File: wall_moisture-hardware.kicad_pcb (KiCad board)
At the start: 4 copper layers, 78.5 x 99.3 mm, 46 parts, among them SW2 FSMH

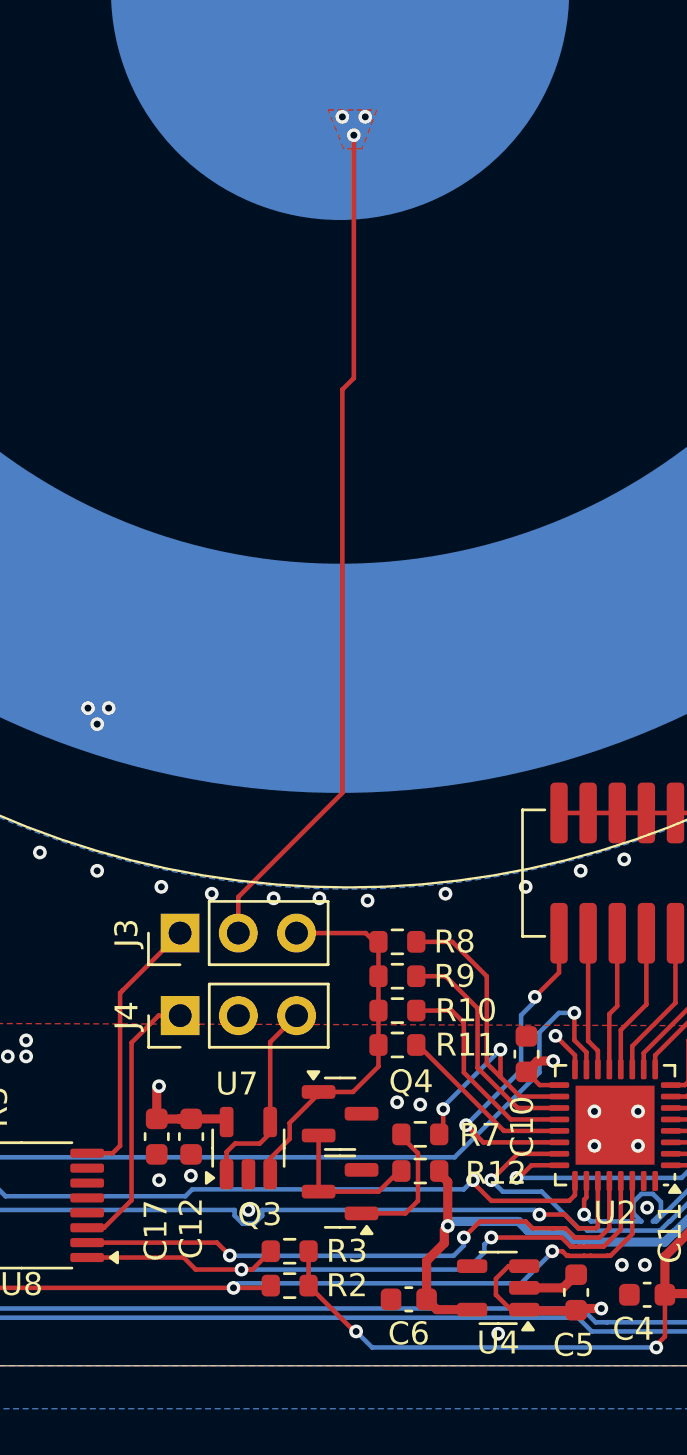
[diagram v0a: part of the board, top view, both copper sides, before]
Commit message: design: Shield excitation signal and exclude poor planes around the signal trace
Excluding poor plane around the signal should reduce the capacitive parasitance.
Shield is now protecting the signal trace that goes to the electrode
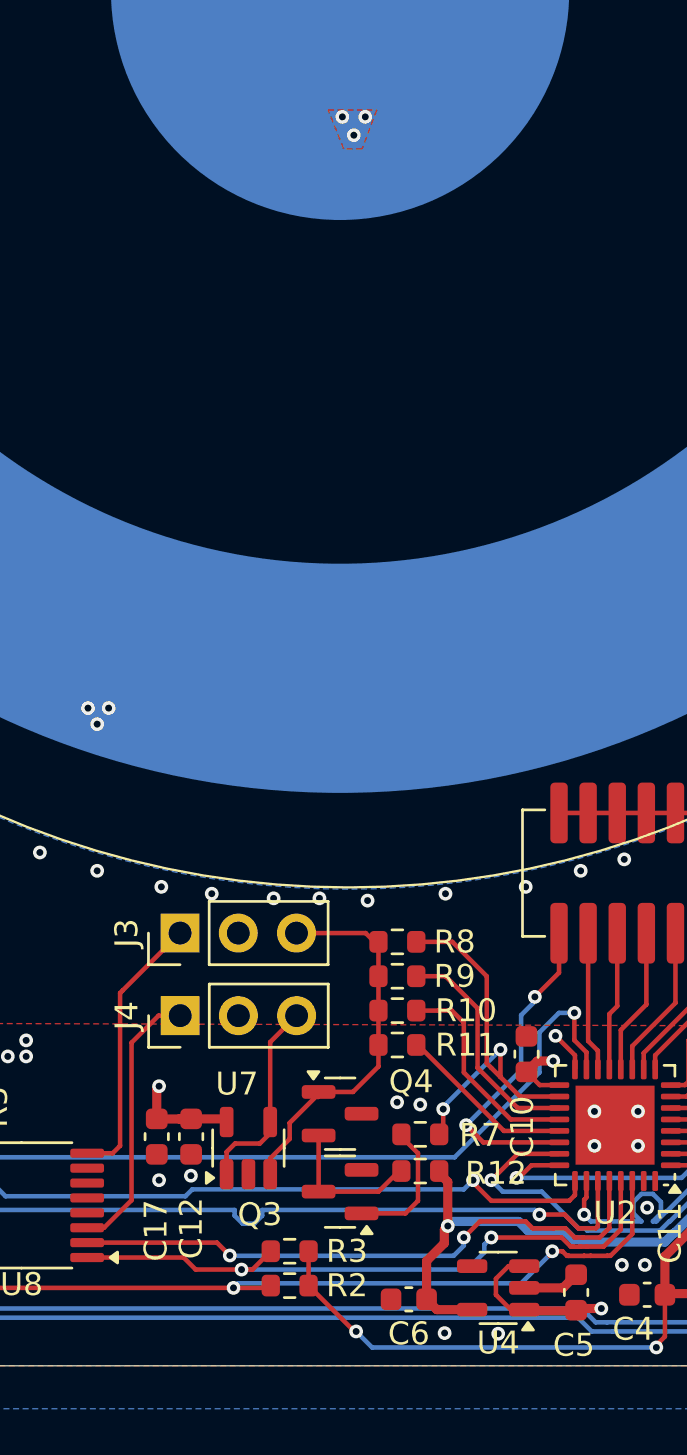
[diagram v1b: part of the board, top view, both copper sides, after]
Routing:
- added copper zone on In1.Cu, net /Analog frontend/SENSOR_SHIELD
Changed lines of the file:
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@@
 	)
 	(via
-		(at 92.338439 132.727778)
+		(at 85.338439 110.827778)
 		(size 0.6)
 		(drill 0.3)
@@
 	)
 	(via
-		(at 85.338439 110.827778)
+		(at 125.538439 125.227778)
 		(size 0.6)
 		(drill 0.3)
@@
 	)
 	(via
-		(at 125.538439 125.227778)
+		(at 66.038439 133.127778)
 		(size 0.6)
 		(drill 0.3)
@@
 	)
 	(via
-		(at 66.038439 133.127778)
+		(at 127.338439 132.527778)
 		(size 0.6)
 		(drill 0.3)
@@
 	)
 	(via
-		(at 127.338439 132.527778)
+		(at 100.9 138.1)
 		(size 0.6)
 		(drill 0.3)
@@
 	)
 	(segment
+		(start 91.896229 120.644614)
+		(end 91.938439 120.602404)
+		(width 0.8)
+		(layer "F.Cu")
+		(net 18)
+	)
+	(via
+		(at 96.938439 85.827778)
+		(size 0.6)
+		(drill 0.3)
+		(layers "F.Cu" "B.Cu")
+		(net 18)
+	)
+	(via
+		(at 97.438439 85.027778)
+		(size 0.6)
+		(drill 0.3)
+		(layers "F.Cu" "B.Cu")
+		(net 18)
+	)
+	(via
+		(at 96.438439 85.027778)
+		(size 0.6)
+		(drill 0.3)
+		(layers "F.Cu" "B.Cu")
+		(net 18)
+	)
+	(segment
 		(start 91.896229 119.069988)
 		(end 96.438439 114.527778)
 		(width 0.2)
-		(layer "F.Cu")
+		(layer "In2.Cu")
 		(net 18)
 	)
@@
 		(end 96.438439 96.927778)
 		(width 0.2)
-		(layer "F.Cu")
+		(layer "In2.Cu")
 		(net 18)
 	)
@@
 		(end 91.896229 119.069988)
 		(width 0.2)
-		(layer "F.Cu")
-		(net 18)
-	)
-	(segment
-		(start 91.896229 120.644614)
-		(end 91.938439 120.602404)
-		(width 0.8)
-		(layer "F.Cu")
+		(layer "In2.Cu")
 		(net 18)
 	)
@@
 		(end 96.938439 86.027778)
 		(width 0.2)
-		(layer "F.Cu")
+		(layer "In2.Cu")
 		(net 18)
 	)
@@
 		(end 96.938439 96.427778)
 		(width 0.2)
-		(layer "F.Cu")
-		(net 18)
-	)
-	(via
-		(at 96.938439 85.827778)
-		(size 0.6)
-		(drill 0.3)
-		(layers "F.Cu" "B.Cu")
-		(net 18)
-	)
-	(via
-		(at 97.438439 85.027778)
-		(size 0.6)
-		(drill 0.3)
-		(layers "F.Cu" "B.Cu")
-		(net 18)
-	)
-	(via
-		(at 96.438439 85.027778)
-		(size 0.6)
-		(drill 0.3)
-		(layers "F.Cu" "B.Cu")
+		(layer "In2.Cu")
 		(net 18)
 	)
@@
 	)
 	(zone
+		(net 0)
+		(net_name "")
+		(layers "F.Cu" "In1.Cu" "In2.Cu")
+		(hatch edge 0.5)
+		(connect_pads
+			(clearance 0)
+		)
+		(min_thickness 0.25)
+		(filled_areas_thickness no)
+		(keepout
+			(tracks allowed)
+			(vias allowed)
+			(pads allowed)
+			(copperpour not_allowed)
+			(footprints allowed)
+		)
+		(placement
+			(enabled no)
+			(sheetname "/Analog frontend/")
+		)
+		(fill
+			(thermal_gap 0.5)
+			(thermal_bridge_width 0.5)
+		)
+		(polygon
+			(pts
+				(xy 83.6 129.5) (xy 83.6 130.8) (xy 87.2 130.8) (xy 87.3 130.7) (xy 87.3 123.8) (xy 89.7 121.4)
+				(xy 90.9 121.4) (xy 90.7 121.2) (xy 87.7 121.2) (xy 85.9 123) (xy 85.9 129.4) (xy 85.8 129.5)
+			)
+		)
+	)
+	(zone
+		(net 0)
+		(net_name "")
+		(layers "F.Cu" "In1.Cu" "In2.Cu")
+		(hatch edge 0.5)
+		(connect_pads
+			(clearance 0)
+		)
+		(min_thickness 0.25)
+		(filled_areas_thickness no)
+		(keepout
+			(tracks allowed)
+			(vias allowed)
+			(pads allowed)
+			(copperpour not_allowed)
+			(footprints allowed)
+		)
+		(placement
+			(enabled no)
+			(sheetname "/Analog frontend/")
+		)
+		(fill
+			(thermal_gap 0.5)
+			(thermal_bridge_width 0.5)
+		)
+		(polygon
+			(pts
+				(xy 93.1 122.4) (xy 93.2 122.5) (xy 97 122.5) (xy 97 126.3) (xy 96.9 126.4) (xy 97.2 126.7) (xy 100.2 126.7)
+				(xy 103 129.5) (xy 106.7 129.5) (xy 106.7 127.3) (xy 106.5 127.1) (xy 104 127.1) (xy 103.9 127)
+				(xy 103.9 124.9) (xy 103.2 124.9) (xy 103.2 121.8) (xy 100.8 119.4) (xy 87.9 119.4) (xy 87.8 119.5)
+				(xy 87.8 122.1) (xy 88.2 122.5) (xy 93.2 122.5)
+			)
+		)
+	)
+	(zone
+		(net 0)
+		(net_name "")
+		(layers "F.Cu" "In1.Cu" "In2.Cu")
+		(hatch edge 0.5)
+		(connect_pads
+			(clearance 0)
+		)
+		(min_thickness 0.25)
+		(filled_areas_thickness no)
+		(keepout
+			(tracks allowed)
+			(vias allowed)
+			(pads allowed)
+			(copperpour not_allowed)
+			(footprints allowed)
+		)
+		(placement
+			(enabled no)
+			(sheetname "/Analog frontend/")
+		)
+		(fill
+			(thermal_gap 0.5)
+			(thermal_bridge_width 0.5)
+		)
+		(polygon
+			(pts
+				(xy 92.8 132.1) (xy 93.7 132.1) (xy 94 131.8) (xy 94 130.3) (xy 94.7 129.6) (xy 94.7 129) (xy 95.8 129)
+				(xy 96.338439 128.461561) (xy 96.338439 128) (xy 97.9 128) (xy 98.9 127) (xy 98.9 126.3) (xy 98.8 126.2)
+				(xy 94.6 126.2) (xy 92.8 128) (xy 92.8 130.8)
+			)
+		)
+	)
+	(zone
 		(net 9)
 		(net_name "/Analog frontend/SENSOR_SHIELD")
@@
 			)
 		)
+	)
+	(zone
+		(net 9)
+		(net_name "/Analog frontend/SENSOR_SHIELD")
+		(layer "In1.Cu")
+		(hatch edge 0.5)
+		(priority 1)
+		(connect_pads
+			(clearance 0.2)
+		)
+		(min_thickness 0.25)
+		(filled_areas_thickness no)
+		(fill yes
+			(thermal_gap 0.5)
+			(thermal_bridge_width 0.5)
+		)
+		(polygon
+			(pts
+				(xy 99.2 83.5) (xy 99.3 114.9) (xy 93.6 121.8) (xy 93.6 125.6) (xy 90 125.6) (xy 90 121.797379)
+				(xy 90.6 118.4) (xy 94.2 113.9) (xy 94.6 83.6)
+			)
+		)

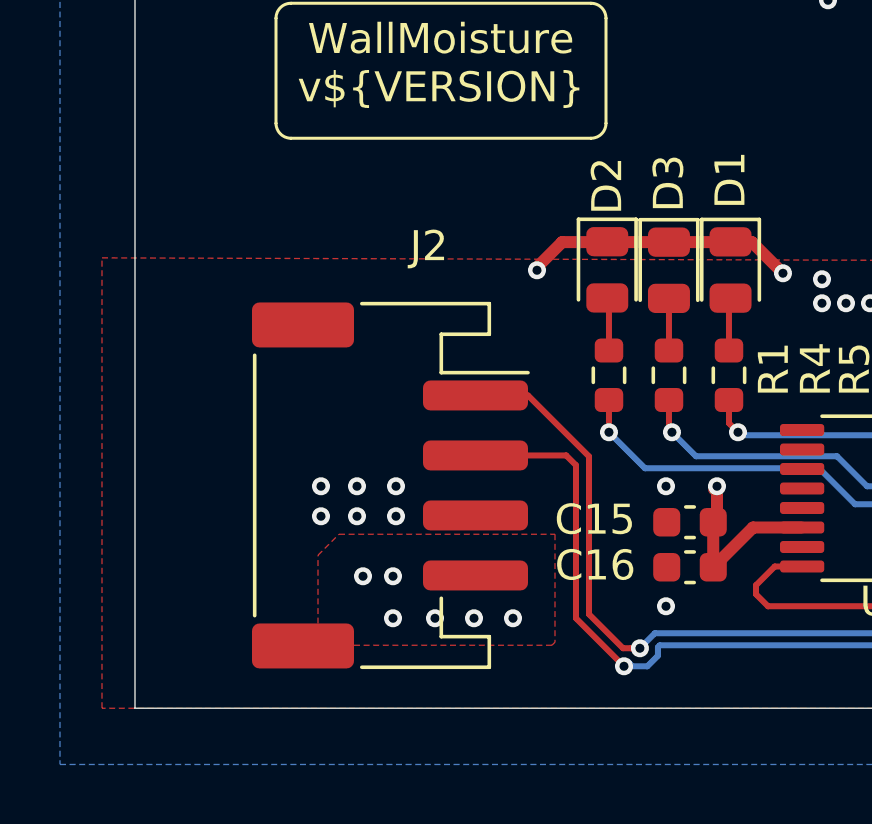
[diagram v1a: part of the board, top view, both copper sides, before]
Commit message: design: Align interface connectors
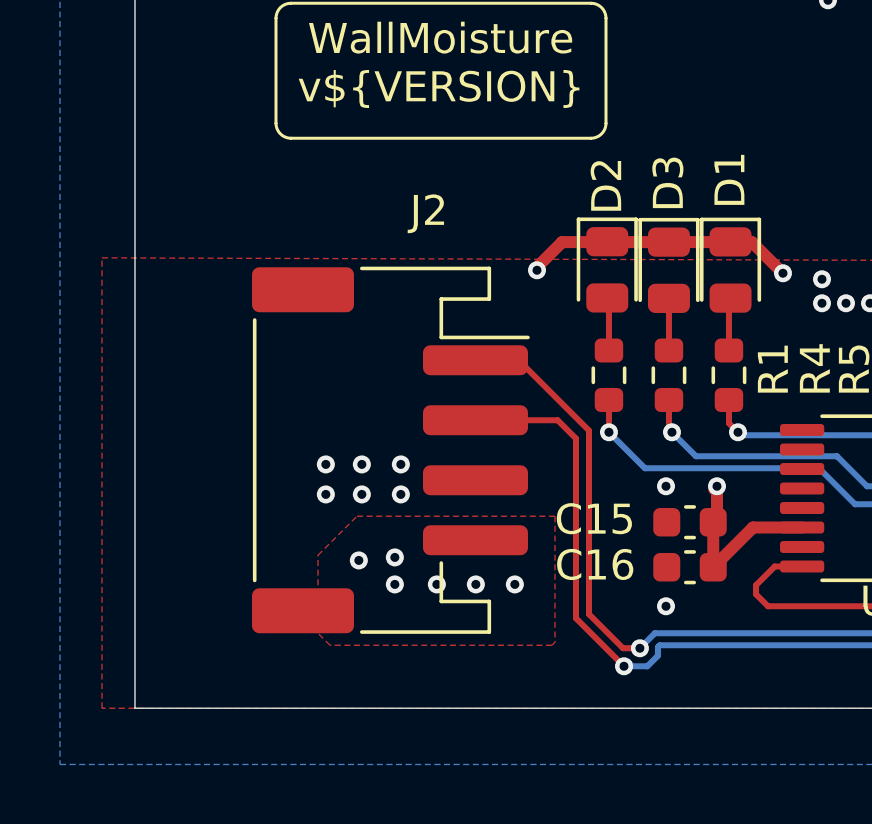
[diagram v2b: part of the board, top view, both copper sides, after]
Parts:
- moved J2 1.17 mm to (65.8, 130.9)
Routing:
- net /Connectors and Power/MASTER_TX: track 91.4 -> 92.4 mm
- net /Connectors and Power/MASTER_RX: track 84.2 -> 85.2 mm
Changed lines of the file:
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@@
 	(footprint "footprints:JST_PH_S4B-PH-SM4-TB_1x04-1MP_P2.00mm_Horizontal"
 		(layer "F.Cu")
-		(at 65.838439 132.101263 -90)
+		(at 65.838439 130.927778 -90)
 		(descr "JST PH series connector, S4B-PH-SM4-TB (http://www.jst-mfg.com/product/pdf/eng/ePH.pdf), generated with kicad-footprint-generator")
 		(tags "connector JST PH horizontal")
 		(property "Reference" "J2"
-			(at -7.973485 -1.3 180)
+			(at -7.973485 -1.3 0)
 			(layer "F.SilkS")
 			(effects
@@
 			(at 0 5.8 90)
 			(layer "F.Fab")
+			(hide yes)
 			(effects
 				(font
@@
 			(layer "F.Fab")
 		)
-		(fp_text user "${REFERENCE}"
-			(at 0 1.5 90)
-			(layer "F.Fab")
-			(effects
-				(font
-					(size 1 1)
-					(thickness 0.15)
-				)
-			)
-		)
 		(pad "1" smd roundrect
 			(at -3 -2.85 270)
@@
 		(sheetname "/Analog frontend/")
 		(sheetfile "analog_front_end.kicad_sch")
-		(attr smd exclude_from_bom dnp)
+		(attr smd exclude_from_bom)
 		(fp_text user "${REFERENCE}"
 			(at 0 -2.5 0)
@@
 	)
 	(via
-		(at 64.738439 132.127778)
+		(at 64.9 131.4)
 		(size 0.6)
 		(drill 0.3)
@@
 	)
 	(via
-		(at 66.038439 133.127778)
+		(at 66.2 132.4)
 		(size 0.6)
 		(drill 0.3)
@@
 	)
 	(via
-		(at 63.538439 133.127778)
+		(at 63.7 132.4)
 		(size 0.6)
 		(drill 0.3)
@@
 	)
 	(via
-		(at 63.538439 132.127778)
+		(at 63.7 131.4)
 		(size 0.6)
 		(drill 0.3)
@@
 	)
 	(via
-		(at 66.038439 132.127778)
+		(at 66.2 131.4)
 		(size 0.6)
 		(drill 0.3)
@@
 	)
 	(via
-		(at 64.738439 133.127778)
+		(at 64.9 132.4)
 		(size 0.6)
 		(drill 0.3)
@@
 	)
 	(via
-		(at 69.938439 136.527778)
+		(at 70 135.4)
 		(size 0.6)
 		(drill 0.3)
@@
 	)
 	(via
-		(at 68.638439 136.527778)
+		(at 68.7 135.4)
 		(size 0.6)
 		(drill 0.3)
@@
 	)
 	(via
-		(at 65.938439 136.527778)
+		(at 66 135.4)
 		(size 0.6)
 		(drill 0.3)
@@
 	)
 	(via
-		(at 65.938439 135.127778)
+		(at 66 134.5)
 		(size 0.6)
 		(drill 0.3)
@@
 	)
 	(via
-		(at 67.338439 136.527778)
+		(at 67.4 135.4)
 		(size 0.6)
 		(drill 0.3)
@@
 	)
 	(via
-		(at 64.938439 135.127778)
+		(at 64.8 134.6)
 		(size 0.6)
 		(drill 0.3)
@@
 	)
 	(segment
-		(start 73.888383 137.527779)
-		(end 73.887382 137.526778)
+		(start 74.168558 137.527779)
+		(end 73.888383 137.527779)
 		(width 0.2)
 		(layer "F.Cu")
@@
 	)
 	(segment
-		(start 74.168558 137.527779)
-		(end 73.888383 137.527779)
+		(start 110.775939 127.277778)
+		(end 111.388439 127.277778)
 		(width 0.2)
 		(layer "F.Cu")
@@
 	)
 	(segment
-		(start 70.438439 129.101263)
-		(end 68.688439 129.101263)
+		(start 72.471989 130.271989)
+		(end 70.127778 127.927778)
 		(width 0.2)
 		(layer "F.Cu")
@@
 	)
 	(segment
-		(start 72.471989 131.134813)
-		(end 70.438439 129.101263)
+		(start 119.914174 133.203513)
+		(end 120.137439 132.980248)
 		(width 0.2)
 		(layer "F.Cu")
@@
 	)
 	(segment
-		(start 73.604539 137.526778)
-		(end 72.471989 136.394228)
+		(start 112.137439 124.728778)
+		(end 117.572339 124.728778)
 		(width 0.2)
 		(layer "F.Cu")
@@
 	)
 	(segment
-		(start 110.775939 127.277778)
-		(end 111.388439 127.277778)
+		(start 111.538439 125.327778)
+		(end 112.137439 124.728778)
 		(width 0.2)
 		(layer "F.Cu")
@@
 	)
 	(segment
-		(start 73.887382 137.526778)
-		(end 73.604539 137.526778)
+		(start 73.888383 137.527779)
+		(end 73.887382 137.526778)
 		(width 0.2)
 		(layer "F.Cu")
@@
 	)
 	(segment
-		(start 119.914174 133.203513)
-		(end 120.137439 132.980248)
+		(start 70.127778 127.927778)
+		(end 68.688439 127.927778)
 		(width 0.2)
 		(layer "F.Cu")
@@
 	)
 	(segment
-		(start 112.137439 124.728778)
-		(end 117.572339 124.728778)
+		(start 120.137439 132.978835)
+		(end 120.489496 132.626778)
 		(width 0.2)
 		(layer "F.Cu")
@@
 	)
 	(segment
-		(start 111.538439 125.327778)
-		(end 112.137439 124.728778)
+		(start 73.887382 137.526778)
+		(end 73.604539 137.526778)
 		(width 0.2)
 		(layer "F.Cu")
@@
 	)
 	(segment
-		(start 120.137439 132.978835)
-		(end 120.489496 132.626778)
+		(start 73.604539 137.526778)
+		(end 72.471989 136.394228)
 		(width 0.2)
 		(layer "F.Cu")
@@
 	(segment
 		(start 72.471989 136.394228)
-		(end 72.471989 131.134813)
+		(end 72.471989 130.271989)
 		(width 0.2)
 		(layer "F.Cu")
@@
 	)
 	(segment
-		(start 73.638439 138.127778)
-		(end 72.038439 136.527778)
+		(start 71.427778 129.927778)
+		(end 68.688439 129.927778)
 		(width 0.2)
 		(layer "F.Cu")
@@
 	)
 	(segment
-		(start 123.438439 129.927778)
-		(end 124.888439 129.927778)
+		(start 73.638439 138.127778)
+		(end 72.038439 136.527778)
 		(width 0.2)
 		(layer "F.Cu")
@@
 	)
 	(segment
-		(start 72.038439 131.427778)
-		(end 71.711924 131.101263)
+		(start 123.438439 129.927778)
+		(end 124.888439 129.927778)
 		(width 0.2)
 		(layer "F.Cu")
@@
 	)
 	(segment
-		(start 71.711924 131.101263)
-		(end 68.688439 131.101263)
+		(start 72.038439 136.527778)
+		(end 72.038439 130.538439)
 		(width 0.2)
 		(layer "F.Cu")
@@
 	)
 	(segment
-		(start 72.038439 136.527778)
-		(end 72.038439 131.427778)
+		(start 120.038439 126.627778)
+		(end 118.988439 125.577778)
 		(width 0.2)
 		(layer "F.Cu")
@@
 	)
 	(segment
-		(start 120.038439 126.627778)
-		(end 118.988439 125.577778)
+		(start 72.038439 130.538439)
+		(end 71.427778 129.927778)
 		(width 0.2)
 		(layer "F.Cu")
@@
 		(polygon
 			(pts
-				(xy 64.138439 133.727778) (xy 71.338439 133.727778) (xy 71.338439 137.327778) (xy 71.238439 137.427778)
+				(xy 64.738439 133.127778) (xy 71.338439 133.127778) (xy 71.338439 137.327778) (xy 71.238439 137.427778)
 				(xy 63.838439 137.427778) (xy 63.438439 137.027778) (xy 63.438439 134.427778)
 			)

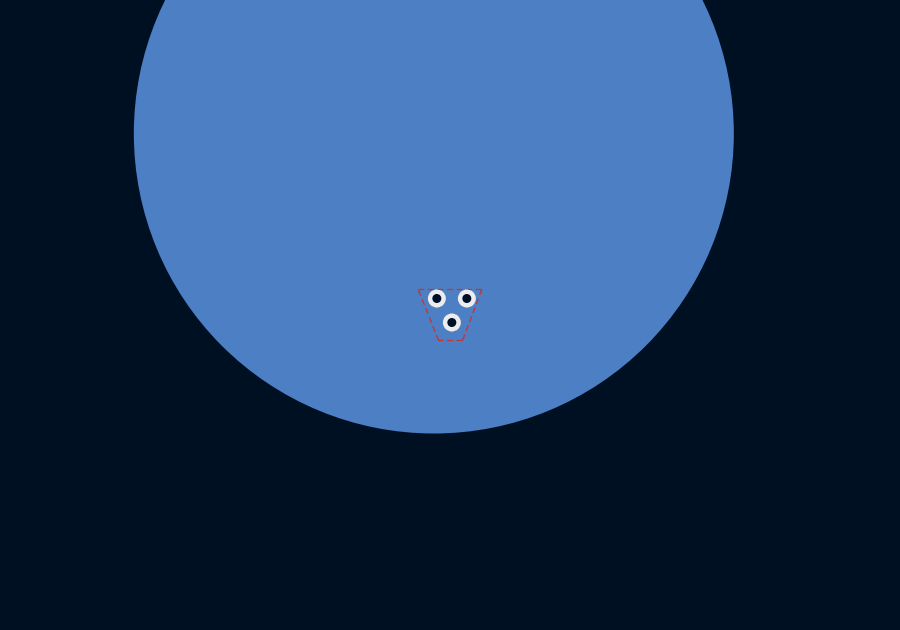
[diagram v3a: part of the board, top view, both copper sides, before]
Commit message: design: Fix signal shielding, move copper pour connecting signal and sensor to the correct layer
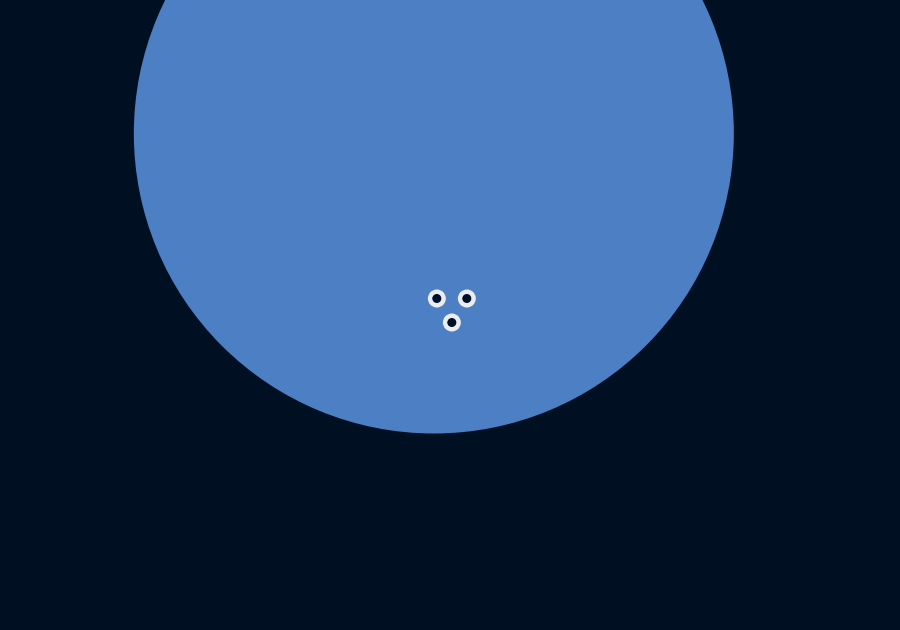
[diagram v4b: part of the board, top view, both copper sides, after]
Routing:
- added copper zone on In2.Cu, net /Analog frontend/SENSOR_EXCITATION
- removed copper zone on F.Cu, net /Analog frontend/SENSOR_EXCITATION
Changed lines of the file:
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@@
-	)
-	(zone
-		(net 18)
-		(net_name "/Analog frontend/SENSOR_EXCITATION")
-		(layer "F.Cu")
-		(hatch edge 0.5)
-		(connect_pads
-			(clearance 0.25)
-		)
-		(min_thickness 0.25)
-		(filled_areas_thickness no)
-		(fill yes
-			(thermal_gap 0.5)
-			(thermal_bridge_width 0.5)
-		)
-		(polygon
-			(pts
-				(xy 95.816217 84.727778) (xy 97.938439 84.727778) (xy 97.296217 86.427778) (xy 96.496217 86.427778)
-			)
-		)
 	)
 	(zone
@@
 			)
 		)
+	)
+	(zone
+		(net 18)
+		(net_name "/Analog frontend/SENSOR_EXCITATION")
+		(layer "In2.Cu")
+		(hatch edge 0.5)
+		(connect_pads
+			(clearance 0.25)
+		)
+		(min_thickness 0.25)
+		(filled_areas_thickness no)
+		(fill yes
+			(thermal_gap 0.5)
+			(thermal_bridge_width 0.5)
+		)
+		(polygon
+			(pts
+				(xy 95.456217 83.827778) (xy 98.6 83.8) (xy 98.1 86.9) (xy 95.9 86.9)
+			)
+		)
